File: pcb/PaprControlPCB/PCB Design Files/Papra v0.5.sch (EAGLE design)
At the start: 33 parts, among them Q1 AO3400A (C20917), U1 LP2985-50DBVR (C74511), U2 ATTINYX04SOIC14

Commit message: Adding schematic for review
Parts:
- removed H4: M-CUI-PJ-066A, PC-LIB:PJ-066A
- added D2, D3: MBR2H100SFT3G C96515, Diode:DIODE_DO-219-AB(SOD123F)
- added F2: 13.2V 1.8A (C70081), SparkFun-Fuses:PPTC_HALF-AMP
- added H2: TE-BNC, PC-LIB:TE-BNC
- added Q2: AO3400A (C20917), Transistor:NMOSFET_BSS123-SOT23
- added R12: 10K 0805W8F1002T5E (C17414), rcl:R-US_R0805
- added R13: 120 0805W8F1200T5E (C17437), rcl:R-US_R0805
- added SG1: YS-MBZ12095DYB12 C409840, buzzer:F/TMB
- D1: value SS34 (C8678) -> MBR2H100SFT3G C96515; device Diode:DIODEDO-214AC(SMA) -> Diode:DIODE_DO-219-AB(SOD123F)
- LED1, LED2, LED3, LED4: value NCD0805R1 (C84256) -> NCD0603G1 C84267
- R3: value 4.7K 0805W8F4701T5E (C17673) -> 1K2 0805W8F1201T5E (C17379)
- R4, R5, R6, R7: value 330 0805W8F3300T5E (C17630) -> 120 0805W8F1200T5E (C17437)
- R8: value 47R 0805W8F470JT5E (C17714) -> 120 0805W8F1200T5E (C17437)
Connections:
- removed net 12V-F: BATT+.PIN@1, BATT+.PIN@2, F1.1, H1.TIP
- removed net FAN-SENSE: H4.RING_SW, U2.PA3/EXTCLK/AIN3/XCK(ALT)/SCK/WO3
- new net 12V-BAT: BATT+.PIN@1, BATT+.PIN@2, D2.A
- new net 12V-DC: D3.A, H1.TIP
- new net 12V-FAN: D1.C, F2.2, H2.P1
- new net BUZZER: R12.2, R13.2, U2.PA3/EXTCLK/AIN3/XCK(ALT)/SCK/WO3
- new net BUZZER-GND: Q2.D, SG1.-
- new net FETGATE1: Q2.G, R13.1
- new net N$2: D2.C, D3.C, F1.1, F2.1
- net +12V: now also SG1.+; no longer D1.C, H4.TIP
- net FAN-GND: now also H2.P2; no longer H4.RING
- net GND: now also Q2.S, R12.1
- net GND-SWITCH: no longer U2.PA4/AIN4/XDIR(ALT)/SS/WO4/LUT-OUT0
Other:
- note added: "BUZZER"
- moved on the sheet: C1, C4, D1, F1, LED5, POT1, Q1, R10, R11, R8, R9

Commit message: V.5 with PCB layout, for review
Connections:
- net N$2 renamed 12V-DIODEOR
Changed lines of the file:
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@@
 <pinref part="D2" gate="G$1" pin="A"/>
 <wire x1="210.82" y1="177.8" x2="213.36" y2="177.8" width="0.1524" layer="91"/>
+<junction x="213.36" y="177.8"/>
 </segment>
 </net>
@@
 </segment>
 </net>
-<net name="N$2" class="1">
+<net name="12V-DIODEOR" class="1">
 <segment>
 <pinref part="D2" gate="G$1" pin="C"/>

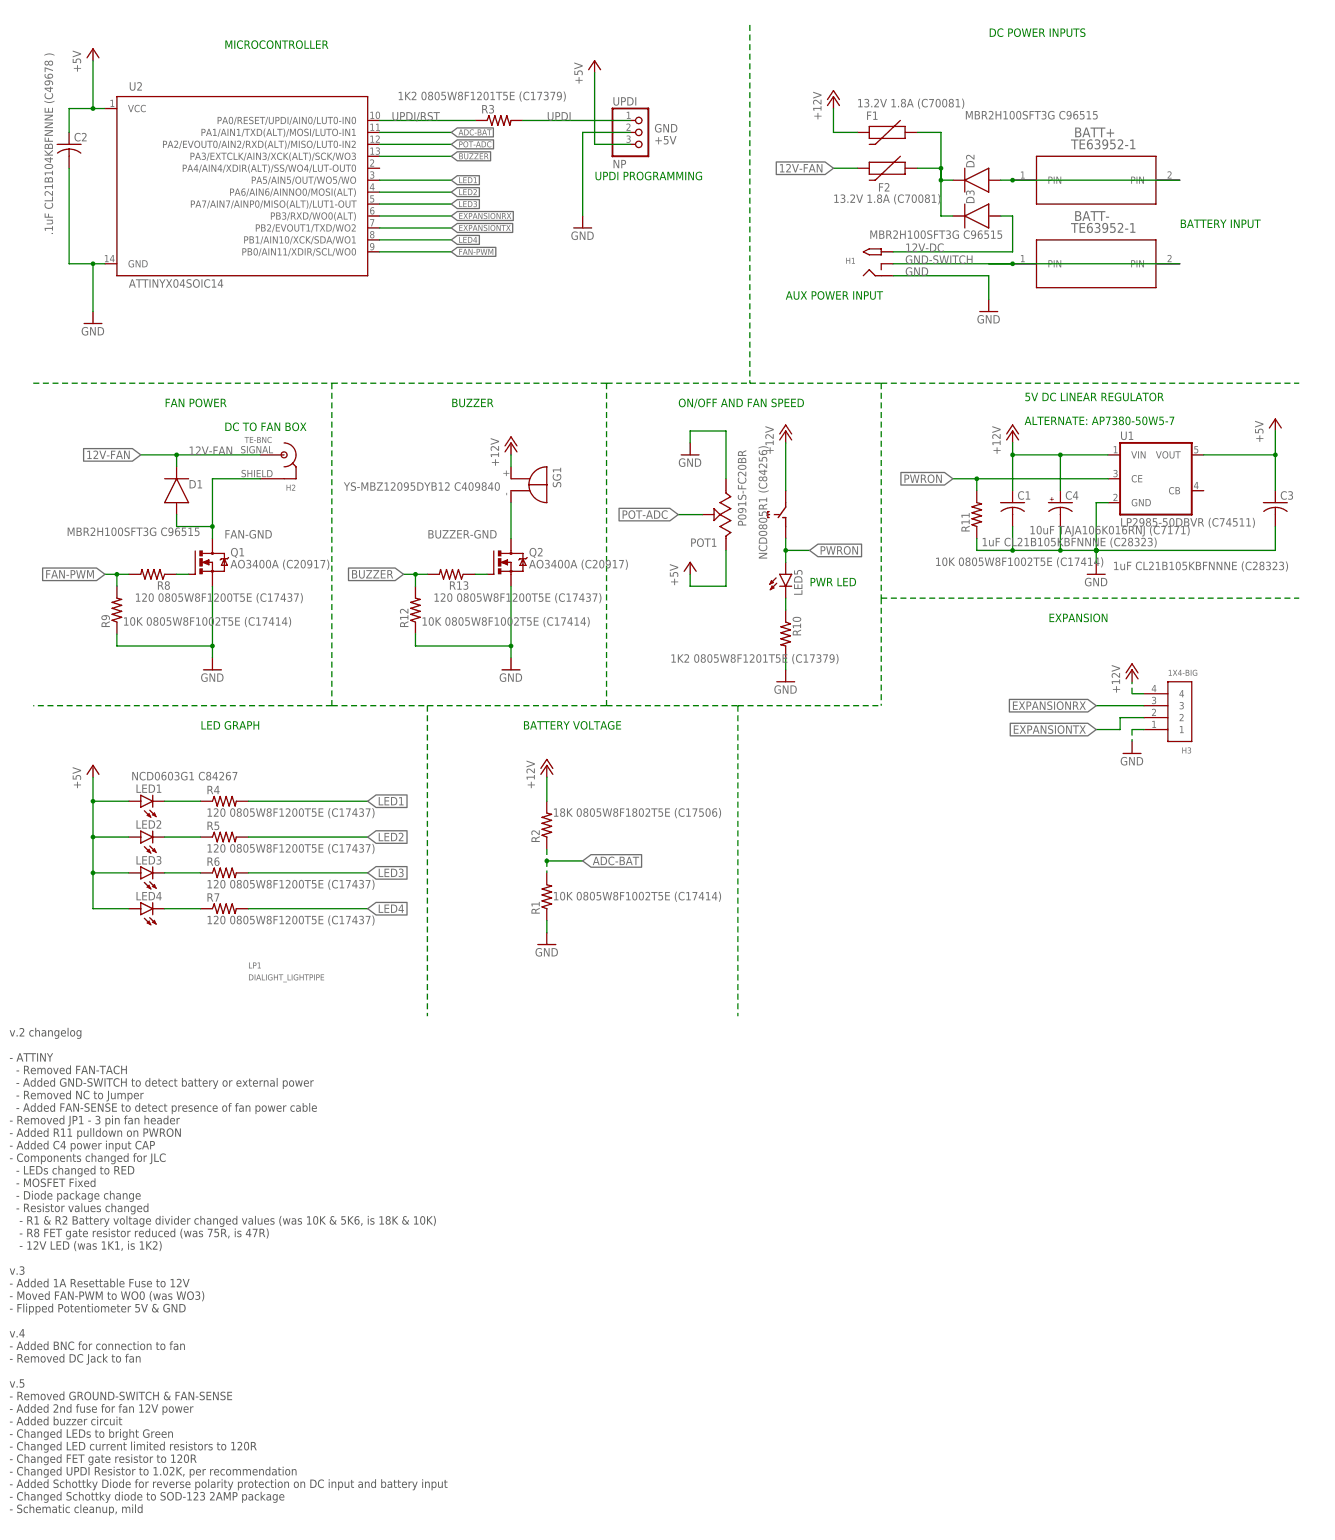
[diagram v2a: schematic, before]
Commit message: Moved Buzzer to W01 & LED4 to PA4
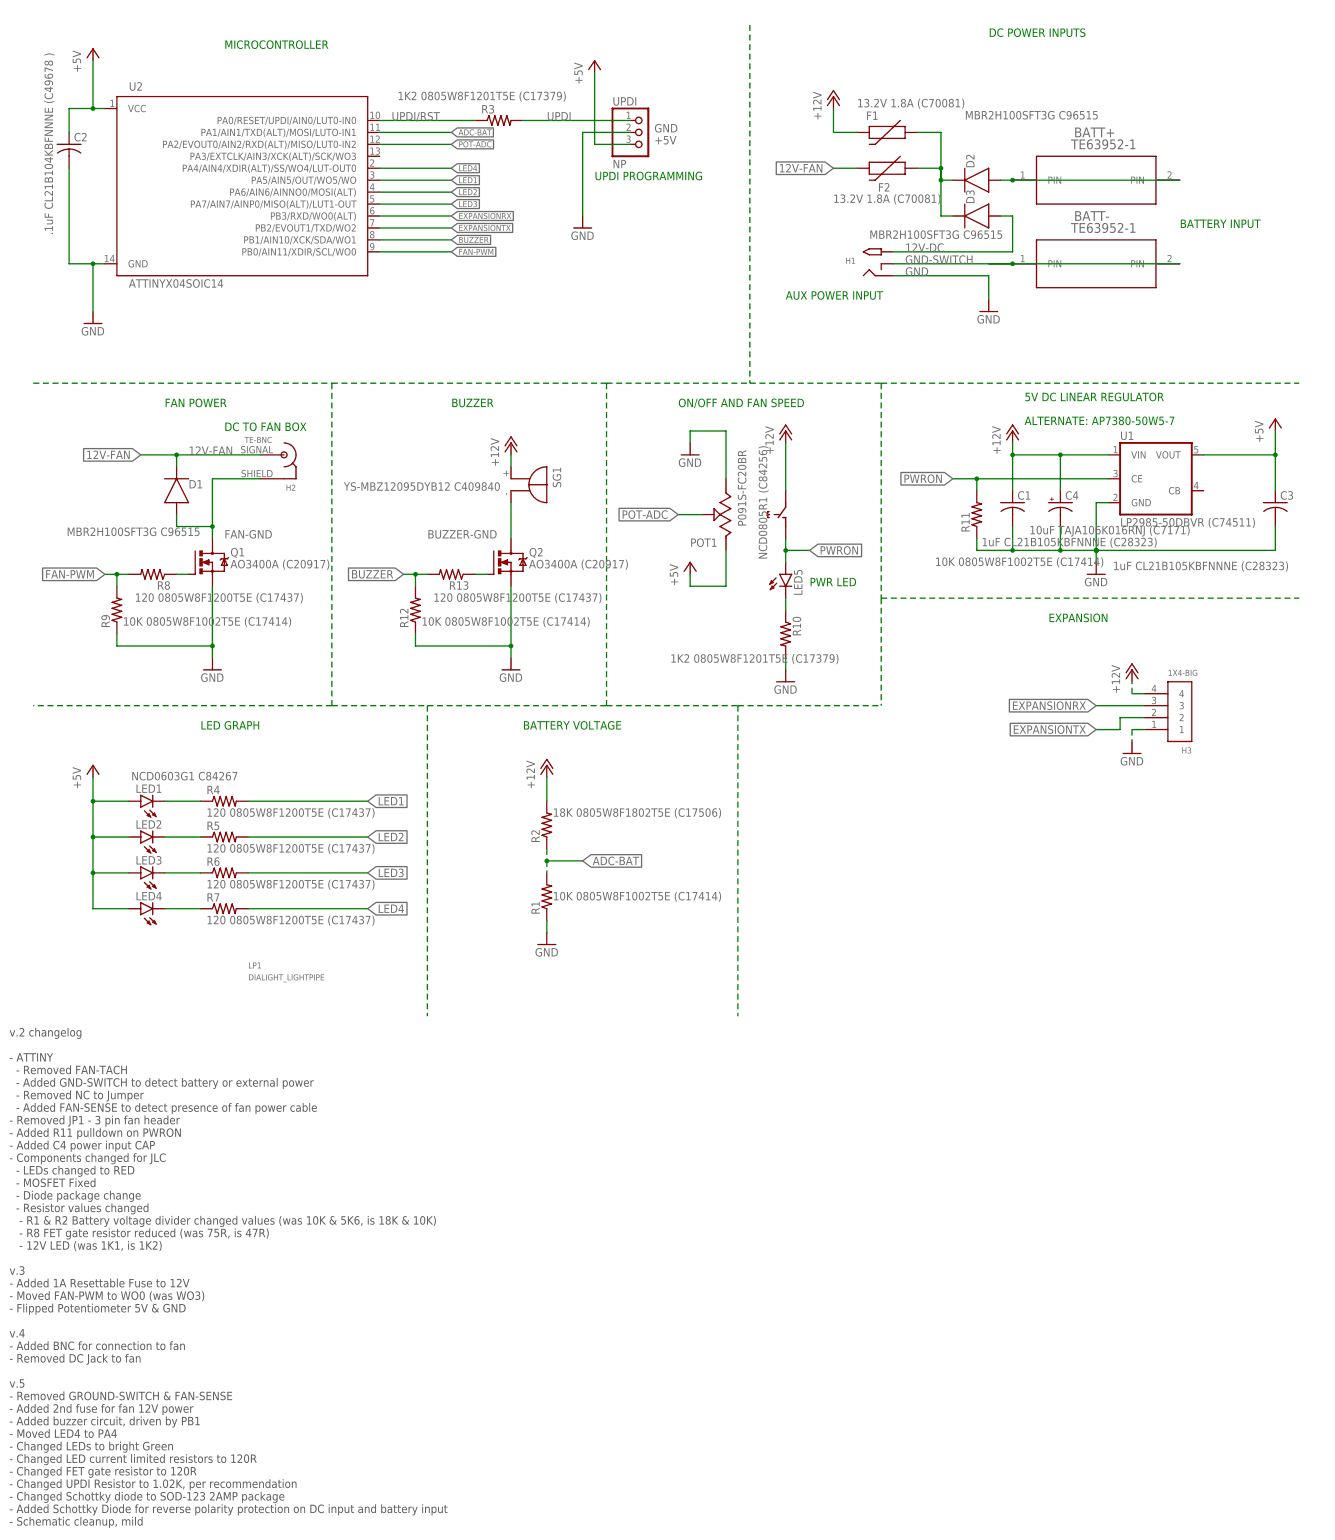
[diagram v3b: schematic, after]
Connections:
- net BUZZER: now also U2.PB1/AIN10/XCK/SDA/WO1; no longer U2.PA3/EXTCLK/AIN3/XCK(ALT)/SCK/WO3
- net LED4: now also U2.PA4/AIN4/XDIR(ALT)/SS/WO4/LUT-OUT0; no longer U2.PB1/AIN10/XCK/SDA/WO1
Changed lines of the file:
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@@
 - Removed GROUND-SWITCH &amp; FAN-SENSE
 - Added 2nd fuse for fan 12V power
-- Added buzzer circuit
+- Added buzzer circuit, driven by PB1
+- Moved LED4 to PA4
 - Changed LEDs to bright Green
 - Changed LED current limited resistors to 120R
 - Changed FET gate resistor to 120R
 - Changed UPDI Resistor to 1.02K, per recommendation
+- Changed Schottky diode to SOD-123 2AMP package
 - Added Schottky Diode for reverse polarity protection on DC input and battery input
-- Changed Schottky diode to SOD-123 2AMP package
 - Schematic cleanup, mild</text>
 <text x="93.98" y="129.54" size="1.778" layer="91">BUZZER</text>
@@
 </segment>
 <segment>
-<pinref part="U2" gate="G$1" pin="PB1/AIN10/XCK/SDA/WO1"/>
-<wire x1="78.74" y1="165.1" x2="93.98" y2="165.1" width="0.1524" layer="91"/>
-<label x="93.98" y="165.1" size="1.27" layer="95" xref="yes"/>
+<wire x1="78.74" y1="180.34" x2="93.98" y2="180.34" width="0.1524" layer="91"/>
+<label x="93.98" y="180.34" size="1.27" layer="95" xref="yes"/>
+<pinref part="U2" gate="G$1" pin="PA4/AIN4/XDIR(ALT)/SS/WO4/LUT-OUT0"/>
 </segment>
 </net>
@@
 </segment>
 <segment>
-<pinref part="U2" gate="G$1" pin="PA3/EXTCLK/AIN3/XCK(ALT)/SCK/WO3"/>
-<wire x1="78.74" y1="182.88" x2="93.98" y2="182.88" width="0.1524" layer="91"/>
-<label x="93.98" y="182.88" size="1.27" layer="95" xref="yes"/>
-</segment>
-</net>
+<wire x1="78.74" y1="165.1" x2="93.98" y2="165.1" width="0.1524" layer="91"/>
+<label x="93.98" y="165.1" size="1.27" layer="95" xref="yes"/>
+<pinref part="U2" gate="G$1" pin="PB1/AIN10/XCK/SDA/WO1"/>
+</segment>
+</net>

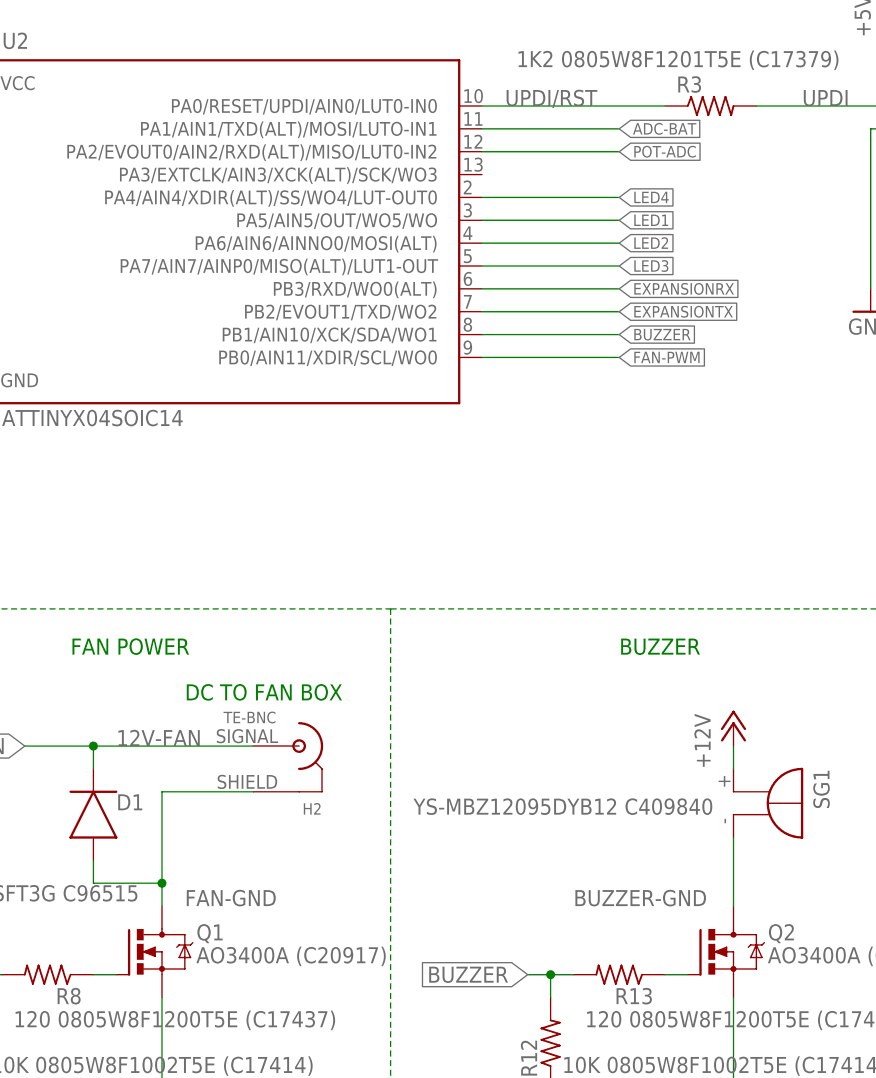
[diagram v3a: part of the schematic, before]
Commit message: Releasing to OSH
- Fixed for JLC DRU
- Unused pin tied to via & labeled PA3
- Adding 2 vias to allow shorting the UPDI resistor for use with programmers that have the UPDI in-circuit
- Tied the posts on the BNC together (can't tie to ground as we are switching ground)
- Silkscreen touchups
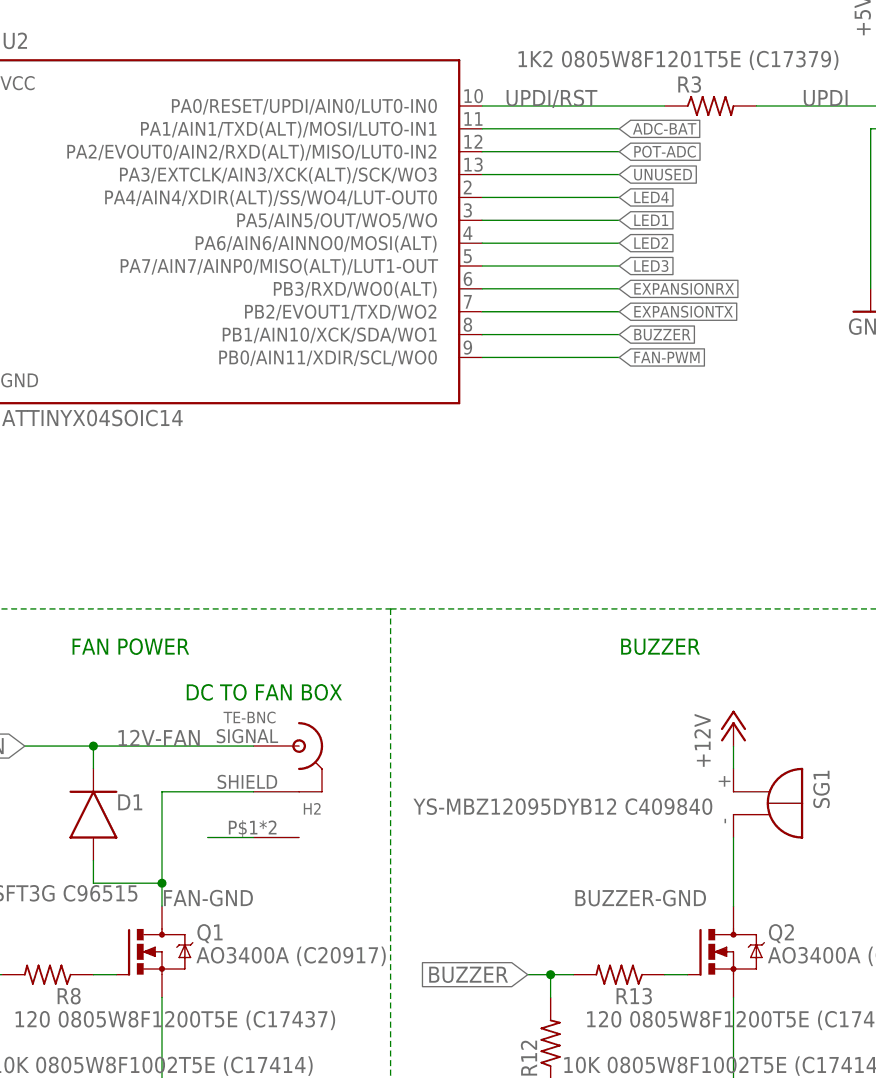
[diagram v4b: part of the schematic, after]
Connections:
- new net PINS: H2.P3
- new net UNUSED: U2.PA3/EXTCLK/AIN3/XCK(ALT)/SCK/WO3
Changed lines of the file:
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@@
 <net name="FAN-GND" class="1">
 <segment>
-<label x="45.72" y="101.6" size="1.778" layer="95"/>
+<label x="43.18" y="101.6" size="1.778" layer="95"/>
 <pinref part="D1" gate="G$1" pin="A"/>
 <wire x1="35.56" y1="106.68" x2="35.56" y2="104.14" width="0.1524" layer="91"/>
@@
 </segment>
 </net>
+<net name="UNUSED" class="0">
+<segment>
+<pinref part="U2" gate="G$1" pin="PA3/EXTCLK/AIN3/XCK(ALT)/SCK/WO3"/>
+<wire x1="78.74" y1="182.88" x2="93.98" y2="182.88" width="0.1524" layer="91"/>
+<label x="93.98" y="182.88" size="1.27" layer="95" xref="yes"/>
+</segment>
+</net>
+<net name="PINS" class="0">
+<segment>
+<pinref part="H2" gate="G$1" pin="P3"/>
+<wire x1="53.34" y1="109.22" x2="48.26" y2="109.22" width="0.1524" layer="91"/>
+</segment>
+</net>

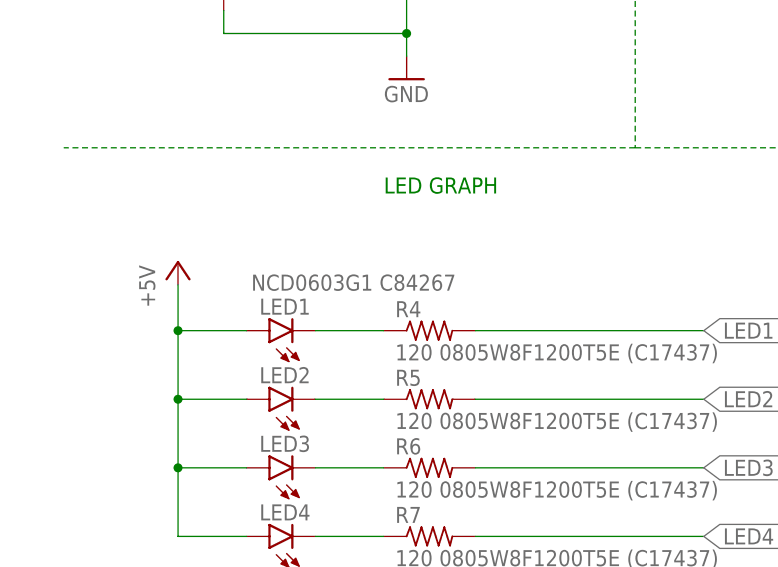
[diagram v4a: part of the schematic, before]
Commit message: File cleanup
Adding in JLC production files, updated BOMs and resolved conflict
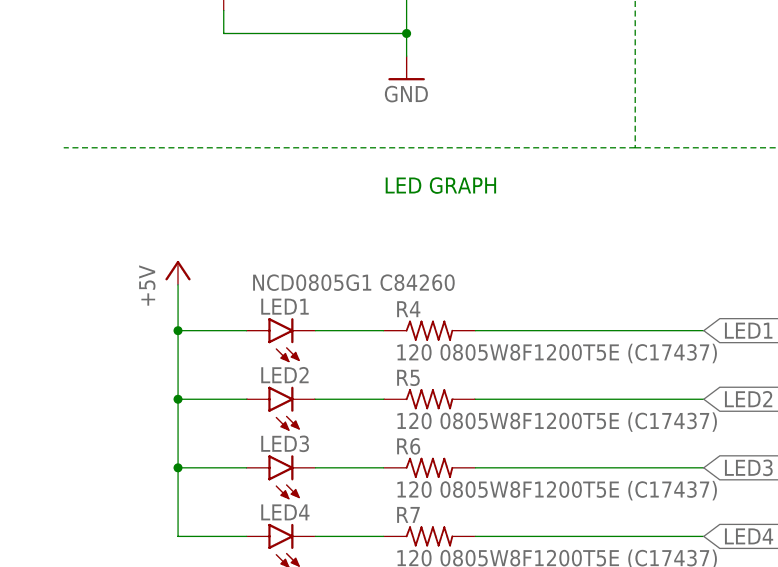
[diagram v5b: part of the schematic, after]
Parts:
- LED1, LED2, LED3, LED4: value NCD0603G1 C84267 -> NCD0805G1 C84260
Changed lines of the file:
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@@
 <part name="D1" library="Diode" library_urn="urn:adsk.eagle:library:16378169" deviceset="DIODE" device="DO-219-AB(SOD123F)" package3d_urn="urn:adsk.eagle:package:9427153/2" technology="_" value="MBR2H100SFT3G C96515"/>
 <part name="H1" library="PC-LIB" deviceset="PJ-066A" device="" value="M-CUI-PJ-066A"/>
-<part name="LED2" library="led" library_urn="urn:adsk.eagle:library:259" deviceset="LED" device="CHIPLED_0805" package3d_urn="urn:adsk.eagle:package:15821/2" value="NCD0603G1 C84267"/>
-<part name="LED3" library="led" library_urn="urn:adsk.eagle:library:259" deviceset="LED" device="CHIPLED_0805" package3d_urn="urn:adsk.eagle:package:15821/2" value="NCD0603G1 C84267"/>
+<part name="LED2" library="led" library_urn="urn:adsk.eagle:library:259" deviceset="LED" device="CHIPLED_0805" package3d_urn="urn:adsk.eagle:package:15821/2" value="NCD0805G1 C84260"/>
+<part name="LED3" library="led" library_urn="urn:adsk.eagle:library:259" deviceset="LED" device="CHIPLED_0805" package3d_urn="urn:adsk.eagle:package:15821/2" value="NCD0805G1 C84260"/>
 <part name="LED5" library="led" library_urn="urn:adsk.eagle:library:259" deviceset="LED" device="CHIPLED_0805" package3d_urn="urn:adsk.eagle:package:15821/2" value="NCD0805R1 (C84256)"/>
-<part name="LED4" library="led" library_urn="urn:adsk.eagle:library:259" deviceset="LED" device="CHIPLED_0805" package3d_urn="urn:adsk.eagle:package:15821/2" value="NCD0603G1 C84267"/>
+<part name="LED4" library="led" library_urn="urn:adsk.eagle:library:259" deviceset="LED" device="CHIPLED_0805" package3d_urn="urn:adsk.eagle:package:15821/2" value="NCD0805G1 C84260"/>
 <part name="R6" library="rcl" library_urn="urn:adsk.eagle:library:334" deviceset="R-US_" device="R0805" package3d_urn="urn:adsk.eagle:package:23553/2" value="120 0805W8F1200T5E (C17437)"/>
 <part name="R5" library="rcl" library_urn="urn:adsk.eagle:library:334" deviceset="R-US_" device="R0805" package3d_urn="urn:adsk.eagle:package:23553/2" value="120 0805W8F1200T5E (C17437)"/>
 <part name="U2" library="PC-LIB" deviceset="ATTINYX04" device="SOIC14" package3d_urn="urn:adsk.eagle:package:9256958/2"/>
-<part name="LED1" library="led" library_urn="urn:adsk.eagle:library:259" deviceset="LED" device="CHIPLED_0805" package3d_urn="urn:adsk.eagle:package:15821/2" value="NCD0603G1 C84267"/>
+<part name="LED1" library="led" library_urn="urn:adsk.eagle:library:259" deviceset="LED" device="CHIPLED_0805" package3d_urn="urn:adsk.eagle:package:15821/2" value="NCD0805G1 C84260"/>
 <part name="R4" library="rcl" library_urn="urn:adsk.eagle:library:334" deviceset="R-US_" device="R0805" package3d_urn="urn:adsk.eagle:package:23553/2" value="120 0805W8F1200T5E (C17437)"/>
 <part name="R10" library="rcl" library_urn="urn:adsk.eagle:library:334" deviceset="R-US_" device="R0805" package3d_urn="urn:adsk.eagle:package:23553/2" value="1K2 0805W8F1201T5E (C17379)"/>
